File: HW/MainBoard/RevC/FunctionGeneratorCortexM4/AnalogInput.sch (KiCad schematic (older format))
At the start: 3 parts, among them U17 THS7001, U18 TS5A3357

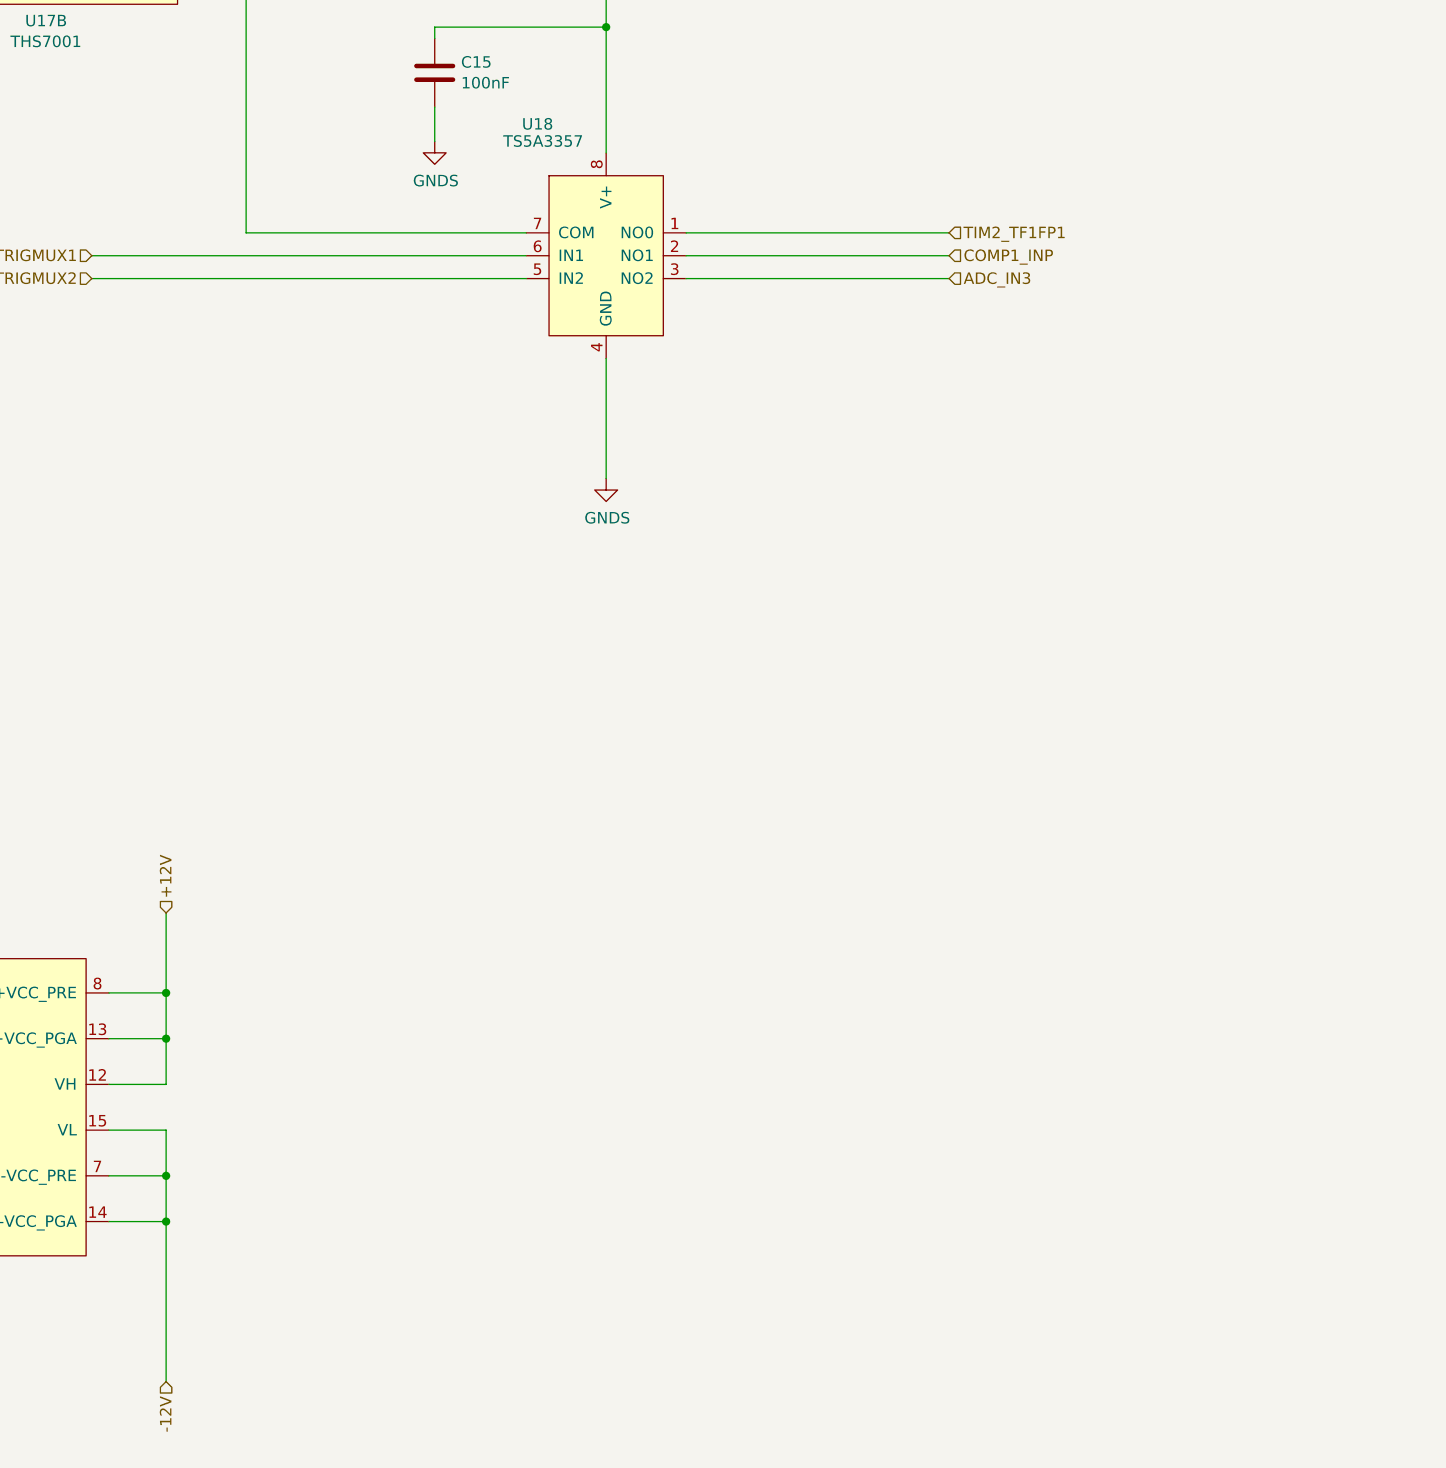
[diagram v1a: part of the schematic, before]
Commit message: Created Front Panel board layout
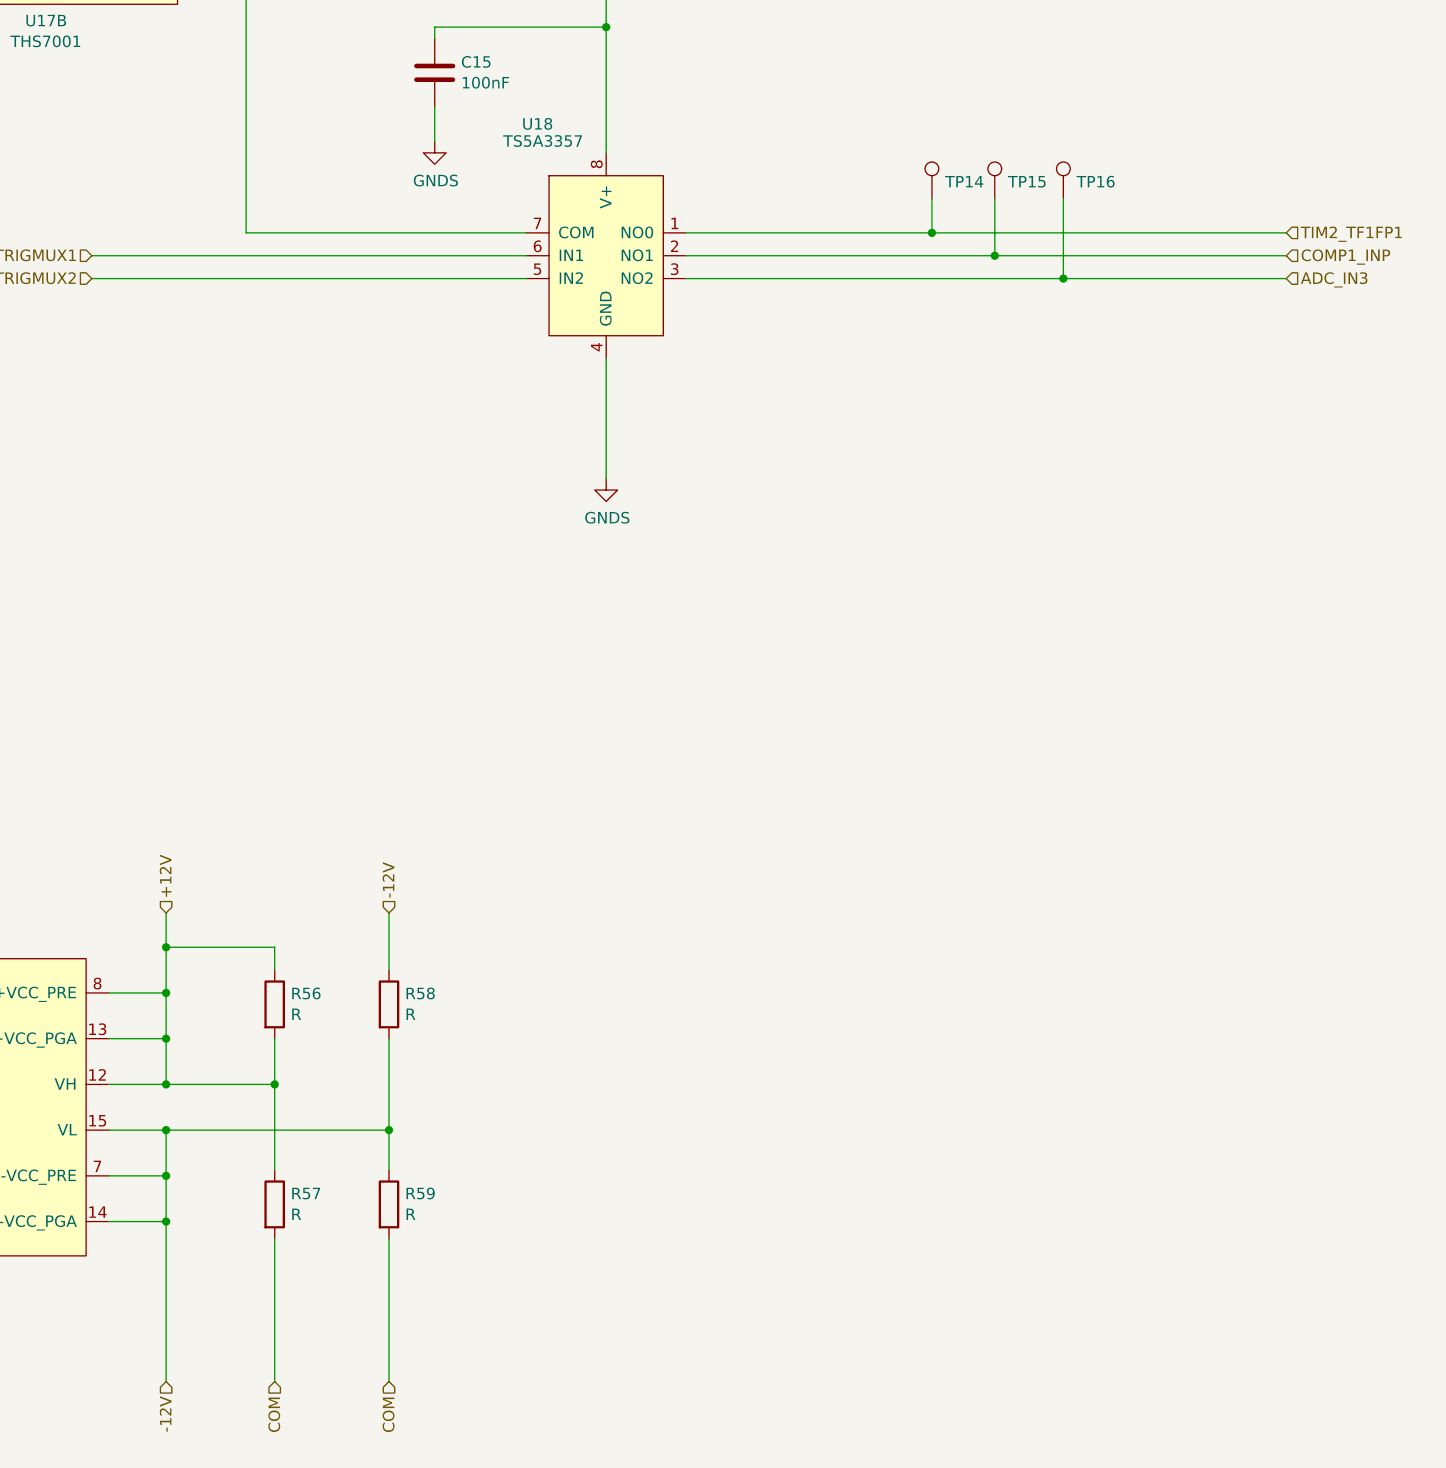
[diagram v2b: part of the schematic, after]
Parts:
- added R56, R57, R58, R59: R, Resistor_SMD:R_0805_2012Metric_Pad1.15x1.40mm_HandSolder, symbol Device:R
- added TP14, TP15, TP16: TestPoint, TestPoint:TestPoint_Pad_1.0x1.0mm, symbol Connector:TestPoint
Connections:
- net +12V: now also R56.1, R56.2, R57.1
- net -12V: now also R58.1, R58.2, R59.1
- net ADC_IN3: now also TP16.1
- net COM: now also R57.2, R59.2
- net COMP1_INP: now also TP15.1
- net TIM2_TF1FP1: now also TP14.1
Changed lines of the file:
@@
 $EndComp
 Wire Wire Line
-	9300 5000 10450 5000
-Wire Wire Line
-	9300 5100 10450 5100
-Wire Wire Line
-	9300 5200 10450 5200
+	9300 5000 10375 5000
+Wire Wire Line
+	9300 5100 10650 5100
+Wire Wire Line
+	9300 5200 10950 5200
 $Comp
 L PGA:THS7001 U?
@@
 +12V
 Wire Wire Line
-	7025 7975 7025 8325
-Text HLabel 10450 5000 2    50   Input ~ 0
+	7025 7975 7025 8125
+Text HLabel 11925 5000 2    50   Input ~ 0
 TIM2_TF1FP1
-Text HLabel 10450 5100 2    50   Input ~ 0
+Text HLabel 11925 5100 2    50   Input ~ 0
 COMP1_INP
-Text HLabel 10450 5200 2    50   Input ~ 0
+Text HLabel 11925 5200 2    50   Input ~ 0
 ADC_IN3
 Text HLabel 6700 5100 0    50   Input ~ 0
@@
 Text HLabel 6500 2475 0    50   Input ~ 0
 INPUT_GAIN_C
+$Comp
+L Connector:TestPoint TP?
+U 1 1 5ED55FC5
+P 10375 4850
+AR Path="/5E5FDE87/5ED55FC5" Ref="TP?"  Part="1"
+AR Path="/5EBB9B06/5ED55FC5" Ref="TP?"  Part="1"
+AR Path="/5F7BA71C/5ED55FC5" Ref="TP14"  Part="1"
+F 0 "TP14" H 10433 4922 50  0000 L CNN
+F 1 "TestPoint" H 10433 4877 50  0001 L CNN
+F 2 "TestPoint:TestPoint_Pad_1.0x1.0mm" H 10575 4850 50  0001 C CNN
+F 3 "~" H 10575 4850 50  0001 C CNN
+	1    10375 4850
+	1    0    0    -1
+$EndComp
+Wire Wire Line
+	10375 4850 10375 5000
+$Comp
+L Connector:TestPoint TP?
+U 1 1 5ED56AD4
+P 10650 4850
+AR Path="/5E5FDE87/5ED56AD4" Ref="TP?"  Part="1"
+AR Path="/5EBB9B06/5ED56AD4" Ref="TP?"  Part="1"
+AR Path="/5F7BA71C/5ED56AD4" Ref="TP15"  Part="1"
+F 0 "TP15" H 10708 4922 50  0000 L CNN
+F 1 "TestPoint" H 10708 4877 50  0001 L CNN
+F 2 "TestPoint:TestPoint_Pad_1.0x1.0mm" H 10850 4850 50  0001 C CNN
+F 3 "~" H 10850 4850 50  0001 C CNN
+	1    10650 4850
+	1    0    0    -1
+$EndComp
+Wire Wire Line
+	10650 4850 10650 5100
+$Comp
+L Connector:TestPoint TP?
+U 1 1 5ED58D1C
+P 10950 4850
+AR Path="/5E5FDE87/5ED58D1C" Ref="TP?"  Part="1"
+AR Path="/5EBB9B06/5ED58D1C" Ref="TP?"  Part="1"
+AR Path="/5F7BA71C/5ED58D1C" Ref="TP16"  Part="1"
+F 0 "TP16" H 11008 4922 50  0000 L CNN
+F 1 "TestPoint" H 11008 4877 50  0001 L CNN
+F 2 "TestPoint:TestPoint_Pad_1.0x1.0mm" H 11150 4850 50  0001 C CNN
+F 3 "~" H 11150 4850 50  0001 C CNN
+	1    10950 4850
+	1    0    0    -1
+$EndComp
+Wire Wire Line
+	10950 4850 10950 5200
+Connection ~ 10375 5000
+Connection ~ 10650 5100
+Connection ~ 10950 5200
+Wire Wire Line
+	10650 5100 11925 5100
+Wire Wire Line
+	10375 5000 11925 5000
+Wire Wire Line
+	10950 5200 11925 5200
+$Comp
+L Device:R R56
+U 1 1 5ED68604
+P 7500 8375
+F 0 "R56" H 7570 8421 50  0000 L CNN
+F 1 "R" H 7570 8330 50  0000 L CNN
+F 2 "Resistor_SMD:R_0805_2012Metric_Pad1.15x1.40mm_HandSolder" V 7430 8375 50  0001 C CNN
+F 3 "~" H 7500 8375 50  0001 C CNN
+	1    7500 8375
+	1    0    0    -1
+$EndComp
+$Comp
+L Device:R R57
+U 1 1 5ED68A55
+P 7500 9250
+F 0 "R57" H 7570 9296 50  0000 L CNN
+F 1 "R" H 7570 9205 50  0000 L CNN
+F 2 "Resistor_SMD:R_0805_2012Metric_Pad1.15x1.40mm_HandSolder" V 7430 9250 50  0001 C CNN
+F 3 "~" H 7500 9250 50  0001 C CNN
+	1    7500 9250
+	1    0    0    -1
+$EndComp
+Wire Wire Line
+	7500 8525 7500 8725
+Wire Wire Line
+	7500 8725 7025 8725
+Connection ~ 7025 8725
+Wire Wire Line
+	7500 8725 7500 9100
+Connection ~ 7500 8725
+Wire Wire Line
+	7500 9400 7500 10025
+Text HLabel 7500 10025 3    50   Input ~ 0
+COM
+Wire Wire Line
+	7500 8225 7500 8125
+Wire Wire Line
+	7500 8125 7025 8125
+Connection ~ 7025 8125
+Wire Wire Line
+	7025 8125 7025 8325
+$Comp
+L Device:R R58
+U 1 1 5ED6C89F
+P 8000 8375
+F 0 "R58" H 8070 8421 50  0000 L CNN
+F 1 "R" H 8070 8330 50  0000 L CNN
+F 2 "Resistor_SMD:R_0805_2012Metric_Pad1.15x1.40mm_HandSolder" V 7930 8375 50  0001 C CNN
+F 3 "~" H 8000 8375 50  0001 C CNN
+	1    8000 8375
+	1    0    0    -1
+$EndComp
+$Comp
+L Device:R R59
+U 1 1 5ED6CB95
+P 8000 9250
+F 0 "R59" H 8070 9296 50  0000 L CNN
+F 1 "R" H 8070 9205 50  0000 L CNN
+F 2 "Resistor_SMD:R_0805_2012Metric_Pad1.15x1.40mm_HandSolder" V 7930 9250 50  0001 C CNN
+F 3 "~" H 8000 9250 50  0001 C CNN
+	1    8000 9250
+	1    0    0    -1
+$EndComp
+Text HLabel 8000 7975 1    50   Input ~ 0
+-12V
+Wire Wire Line
+	8000 7975 8000 8225
+Wire Wire Line
+	8000 8525 8000 8925
+Wire Wire Line
+	7025 8925 8000 8925
+Connection ~ 7025 8925
+Connection ~ 8000 8925
+Wire Wire Line
+	8000 8925 8000 9100
+Wire Wire Line
+	8000 9400 8000 10025
+Text HLabel 8000 10025 3    50   Input ~ 0
+COM
 $EndSCHEMATC

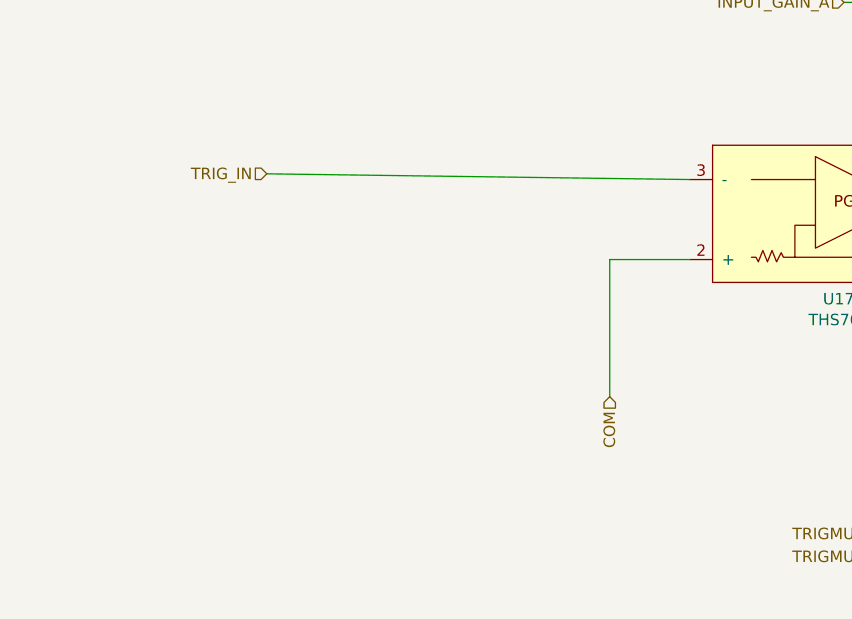
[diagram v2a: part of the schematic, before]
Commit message: update analog input schema
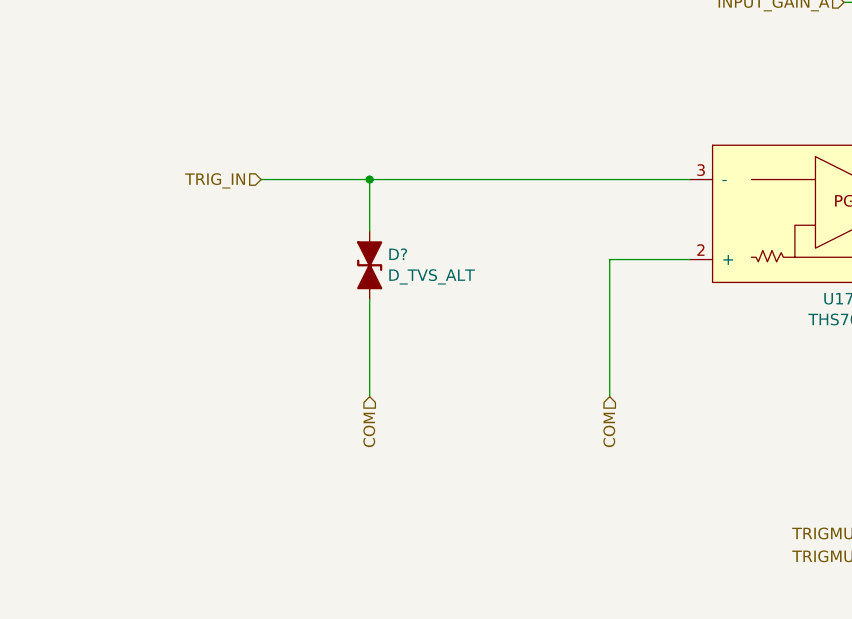
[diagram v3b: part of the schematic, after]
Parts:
- added D?: D_TVS_ALT, Diode_SMD:D_SMA_Handsoldering, symbol Device:D_TVS_ALT
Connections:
- net COM: now also D?.2 (A2)
- net TRIG_IN: now also D?.1 (A1)
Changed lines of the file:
@@
 	1    0    0    -1
 $EndComp
-Text HLabel 3975 3525 0    50   Input ~ 0
+Text HLabel 3950 3550 0    50   Input ~ 0
 TRIG_IN
 $Comp
@@
 $EndComp
 Wire Wire Line
-	3975 3525 5825 3550
+	3950 3550 4425 3550
 Wire Wire Line
 	7175 3650 7375 3650
@@
 Text HLabel 8000 10025 3    50   Input ~ 0
 COM
+$Comp
+L Device:D_TVS_ALT D?
+U 1 1 5ED70DB7
+P 4425 3925
+F 0 "D?" V 4379 4004 50  0000 L CNN
+F 1 "D_TVS_ALT" V 4470 4004 50  0000 L CNN
+F 2 "Diode_SMD:D_SMA_Handsoldering" H 4425 3925 50  0001 C CNN
+F 3 "https://www.mouser.co.uk/datasheet/2/240/Littelfuse_TVS_Diode_P4SMA_Datasheet.pdf-540735.pdf" H 4425 3925 50  0001 C CNN
+	1    4425 3925
+	0    1    1    0
+$EndComp
+Wire Wire Line
+	4425 3775 4425 3550
+Connection ~ 4425 3550
+Wire Wire Line
+	4425 3550 5825 3550
+Wire Wire Line
+	4425 4075 4425 4500
+Text HLabel 4425 4500 3    50   Input ~ 0
+COM
 $EndSCHEMATC
